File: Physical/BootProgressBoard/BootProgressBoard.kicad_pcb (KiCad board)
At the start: 2 copper layers, 49.5 x 28.6 mm, 12 parts, among them P1 CONN_01X09

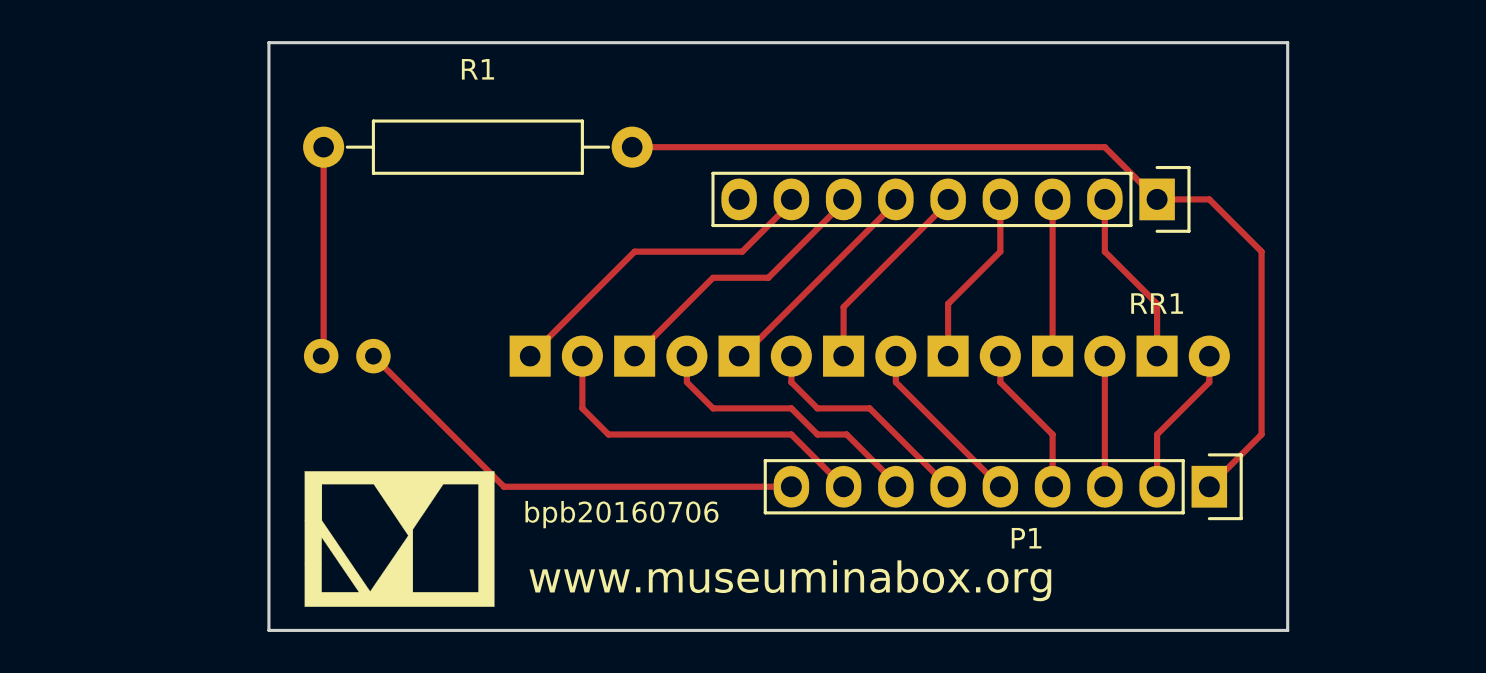
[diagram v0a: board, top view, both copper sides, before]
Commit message: Drop www. from URL, move logo & URL
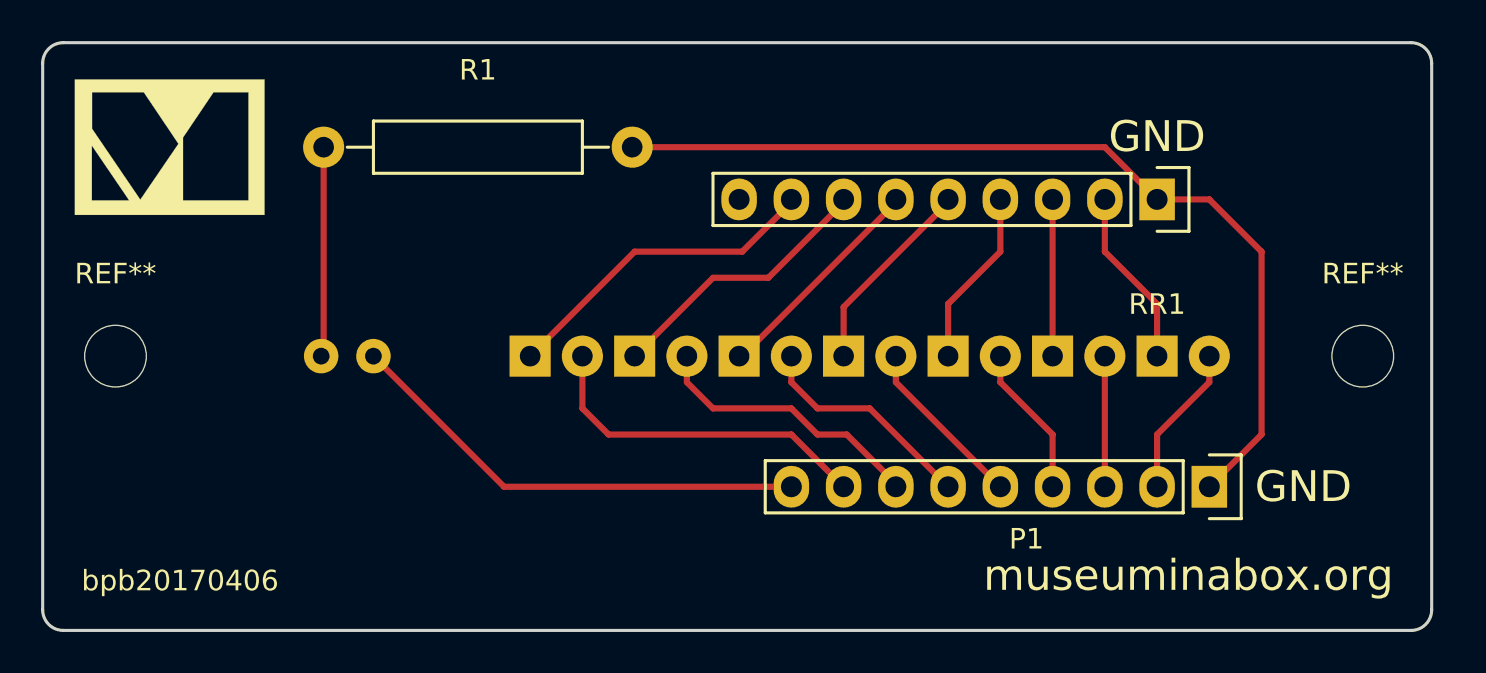
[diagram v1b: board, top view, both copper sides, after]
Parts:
- added G***: LOGO, MCQN Ltd:miab-logo-9x7mm, B.Cu at (154.4, 43.2)
- added REF**: MountingHole_3mm, Mounting_Holes:MountingHole_3mm, F.Cu at (96.7, 53.3)
- added REF**: MountingHole_3mm, Mounting_Holes:MountingHole_3mm, F.Cu at (157.3, 53.3)
- moved G*** 22.1 mm to (99.3, 43.2)
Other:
- board size 49.5 x 28.6 mm -> 67.5 x 28.6 mm
- board text added: "GND"
- board text added: "bpb20170406"
- board text added: "museuminabox.org"
- board text removed: "bpb20160706"
- board text removed: "www.museuminabox.org"
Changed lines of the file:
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@@
-(kicad_pcb (version 4) (host pcbnew 4.1.0-alpha+201607021448+6961~45~ubuntu15.04.1-product)
+(kicad_pcb (version 20170123) (host pcbnew no-vcs-found-1e25c47~58~ubuntu16.04.1)
   (general
-    (links 0)
+    (links 18)
     (no_connects 0)
-    (area 103.864999 38.024999 153.745001 66.750001)
+    (area 90.191475 38.024999 165.810046 66.750001)
     (thickness 1.6)
-    (drawings 6)
+    (drawings 13)
     (tracks 55)
     (zones 0)
-    (modules 12)
+    (modules 15)
     (nets 19)
   )
@@
     (trace_min 0.2)
     (segment_width 0.2)
-    (edge_width 0.15)
+    (edge_width 0.2)
     (via_size 0.8)
     (via_drill 0.4)
@@
     (add_net "Net-(RR1-Pad9)")
   )
+  (module Mounting_Holes:MountingHole_3mm (layer F.Cu)
+    (at 96.68 53.34)
+    (descr "Mounting hole, Befestigungsbohrung, 3mm, No Annular, Kein Restring,")
+    (tags "Mounting hole, Befestigungsbohrung, 3mm, No Annular, Kein Restring,")
+    (fp_text reference REF** (at 0 -4.0005) (layer F.SilkS)
+      (effects (font (size 1 1) (thickness 0.15)))
+    )
+    (fp_text value MountingHole_3mm (at 1.00076 5.00126) (layer F.Fab)
+      (effects (font (size 1 1) (thickness 0.15)))
+    )
+    (fp_circle (center 0 0) (end 3 0) (layer Cmts.User) (width 0.381))
+    (pad 1 thru_hole circle (at 0 0) (size 3 3) (drill 3) (layers))
+  )
+  (module Mounting_Holes:MountingHole_3mm (layer F.Cu)
+    (at 157.32 53.34)
+    (descr "Mounting hole, Befestigungsbohrung, 3mm, No Annular, Kein Restring,")
+    (tags "Mounting hole, Befestigungsbohrung, 3mm, No Annular, Kein Restring,")
+    (fp_text reference REF** (at 0 -4.0005) (layer F.SilkS)
+      (effects (font (size 1 1) (thickness 0.15)))
+    )
+    (fp_text value MountingHole_3mm (at 1.00076 5.00126) (layer F.Fab)
+      (effects (font (size 1 1) (thickness 0.15)))
+    )
+    (fp_circle (center 0 0) (end 3 0) (layer Cmts.User) (width 0.381))
+    (pad 1 thru_hole circle (at 0 0) (size 3 3) (drill 3) (layers))
+  )
+  (module "MCQN Ltd:miab-logo-9x7mm" (layer B.Cu)
+    (at 154.432 43.18 180)
+    (fp_text reference G*** (at 0 0 180) (layer B.SilkS) hide
+      (effects (font (thickness 0.3)) (justify mirror))
+    )
+    (fp_text value LOGO (at 0.75 0 180) (layer B.SilkS) hide
+      (effects (font (thickness 0.3)) (justify mirror))
+    )
+    (fp_poly (pts (xy 4.611512 -3.293533) (xy -4.608688 -3.293533) (xy -4.608688 -1.255324) (xy -3.7846 -1.255324)
+      (xy -3.7846 -2.587977) (xy -1.969262 -2.587977) (xy -1.973457 -2.581627) (xy -1.976057 -2.577762)
+      (xy -1.981691 -2.569442) (xy -1.990252 -2.556826) (xy -2.001629 -2.540074) (xy -2.015714 -2.519346)
+      (xy -2.032398 -2.494802) (xy -2.051573 -2.466603) (xy -2.073129 -2.434907) (xy -2.096958 -2.399875)
+      (xy -2.122951 -2.361666) (xy -2.150998 -2.32044) (xy -2.180992 -2.276358) (xy -2.212823 -2.229579)
+      (xy -2.246382 -2.180263) (xy -2.281561 -2.128569) (xy -2.318251 -2.074658) (xy -2.356342 -2.01869)
+      (xy -2.395727 -1.960824) (xy -2.436296 -1.901221) (xy -2.477941 -1.840039) (xy -2.520551 -1.777439)
+      (xy -2.56402 -1.713582) (xy -2.608238 -1.648626) (xy -2.653095 -1.582731) (xy -2.698484 -1.516058)
+      (xy -2.744295 -1.448767) (xy -2.790419 -1.381016) (xy -2.836749 -1.312966) (xy -2.883174 -1.244778)
+      (xy -2.929586 -1.17661) (xy -2.975876 -1.108622) (xy -3.021935 -1.040975) (xy -3.067655 -0.973829)
+      (xy -3.112927 -0.907342) (xy -3.157641 -0.841676) (xy -3.201689 -0.77699) (xy -3.244963 -0.713443)
+      (xy -3.287353 -0.651196) (xy -3.32875 -0.590408) (xy -3.369045 -0.53124) (xy -3.408131 -0.473851)
+      (xy -3.445897 -0.418401) (xy -3.482235 -0.36505) (xy -3.517037 -0.313958) (xy -3.550193 -0.265285)
+      (xy -3.581594 -0.21919) (xy -3.611132 -0.175833) (xy -3.638698 -0.135375) (xy -3.664183 -0.097975)
+      (xy -3.687478 -0.063793) (xy -3.708475 -0.032988) (xy -3.727064 -0.005722) (xy -3.743137 0.017847)
+      (xy -3.756584 0.037559) (xy -3.767297 0.053253) (xy -3.775168 0.06477) (xy -3.780087 0.07195)
+      (xy -3.781945 0.074634) (xy -3.781957 0.074648) (xy -3.782166 0.072056) (xy -3.782367 0.063907)
+      (xy -3.782562 0.050287) (xy -3.782748 0.031283) (xy -3.782927 0.006984) (xy -3.783097 -0.022526)
+      (xy -3.78326 -0.057158) (xy -3.783414 -0.096825) (xy -3.783559 -0.141441) (xy -3.783696 -0.190918)
+      (xy -3.783823 -0.24517) (xy -3.783942 -0.304109) (xy -3.784052 -0.367649) (xy -3.784152 -0.435702)
+      (xy -3.784242 -0.508182) (xy -3.784323 -0.585002) (xy -3.784393 -0.666074) (xy -3.784454 -0.751312)
+      (xy -3.784504 -0.840628) (xy -3.784544 -0.933936) (xy -3.784574 -1.031148) (xy -3.784592 -1.132178)
+      (xy -3.784599 -1.236939) (xy -3.7846 -1.255324) (xy -4.608688 -1.255324) (xy -4.608688 0.897932)
+      (xy -3.773311 0.897932) (xy -2.629958 -0.783639) (xy -2.569622 -0.872377) (xy -2.509994 -0.960073)
+      (xy -2.451157 -1.046605) (xy -2.393193 -1.131853) (xy -2.336183 -1.215697) (xy -2.280209 -1.298017)
+      (xy -2.225353 -1.378691) (xy -2.171698 -1.457601) (xy -2.119324 -1.534624) (xy -2.068314 -1.609641)
+      (xy -2.01875 -1.682532) (xy -1.970713 -1.753175) (xy -1.924286 -1.82145) (xy -1.87955 -1.887238)
+      (xy -1.836588 -1.950417) (xy -1.79548 -2.010867) (xy -1.75631 -2.068468) (xy -1.719159 -2.123099)
+      (xy -1.684109 -2.17464) (xy -1.651241 -2.222971) (xy -1.620639 -2.26797) (xy -1.592382 -2.309518)
+      (xy -1.566555 -2.347493) (xy -1.543238 -2.381777) (xy -1.522512 -2.412247) (xy -1.504462 -2.438785)
+      (xy -1.489167 -2.461268) (xy -1.47671 -2.479578) (xy -1.467173 -2.493593) (xy -1.460638 -2.503193)
+      (xy -1.457187 -2.508257) (xy -1.457017 -2.508506) (xy -1.447611 -2.52199) (xy -1.43921 -2.533505)
+      (xy -1.43234 -2.542373) (xy -1.427529 -2.547912) (xy -1.425306 -2.549441) (xy -1.425294 -2.549429)
+      (xy -1.423592 -2.546979) (xy -1.418799 -2.539996) (xy -1.411003 -2.528609) (xy -1.400291 -2.512949)
+      (xy -1.386754 -2.493144) (xy -1.370479 -2.469326) (xy -1.351554 -2.441622) (xy -1.33007 -2.410164)
+      (xy -1.306113 -2.375081) (xy -1.279772 -2.336503) (xy -1.251137 -2.294559) (xy -1.220296 -2.249379)
+      (xy -1.187337 -2.201094) (xy -1.152348 -2.149832) (xy -1.115419 -2.095723) (xy -1.076638 -2.038898)
+      (xy -1.036094 -1.979486) (xy -0.993874 -1.917617) (xy -0.950068 -1.85342) (xy -0.904765 -1.787026)
+      (xy -0.858052 -1.718563) (xy -0.810018 -1.648163) (xy -0.760753 -1.575954) (xy -0.710343 -1.502066)
+      (xy -0.658879 -1.42663) (xy -0.606449 -1.349774) (xy -0.55314 -1.271629) (xy -0.499042 -1.192324)
+      (xy -0.49845 -1.191456) (xy 0.426258 0.164143) (xy 0.377524 0.23677) (xy 0.37286 0.243715)
+      (xy 0.365146 0.255192) (xy 0.354486 0.271049) (xy 0.340981 0.291135) (xy 0.324732 0.315298)
+      (xy 0.305842 0.343388) (xy 0.284412 0.375252) (xy 0.260544 0.410739) (xy 0.234341 0.449698)
+      (xy 0.223481 0.465845) (xy 0.649112 0.465845) (xy 0.649112 -2.587977) (xy 3.832578 -2.587977)
+      (xy 3.832578 2.667) (xy 2.131737 2.667) (xy 1.390424 1.566423) (xy 0.649112 0.465845)
+      (xy 0.223481 0.465845) (xy 0.205903 0.491978) (xy 0.175333 0.537426) (xy 0.142733 0.585892)
+      (xy 0.108205 0.637223) (xy 0.07185 0.69127) (xy 0.03377 0.747879) (xy -0.005932 0.8069)
+      (xy -0.047156 0.868182) (xy -0.089799 0.931572) (xy -0.133759 0.99692) (xy -0.178934 1.064074)
+      (xy -0.225223 1.132882) (xy -0.272524 1.203194) (xy -0.320734 1.274857) (xy -0.369753 1.347721)
+      (xy -0.419477 1.421633) (xy -0.464255 1.488192) (xy -1.2573 2.666986) (xy -2.515305 2.666993)
+      (xy -3.773311 2.667) (xy -3.773311 0.897932) (xy -4.608688 0.897932) (xy -4.608688 3.290711)
+      (xy 4.611512 3.290711) (xy 4.611512 -3.293533)) (layer B.SilkS) (width 0.01))
+  )
   (module LEDs:LED-8MM (layer B.Cu)
     (at 106.68 53.34)
@@
   )
   (module "MCQN Ltd:miab-logo-9x7mm" (layer F.Cu)
-    (at 110.49 62.23)
+    (at 99.314 43.18)
     (fp_text reference G*** (at 0 0) (layer F.SilkS) hide
       (effects (font (thickness 0.3)))
@@
       (xy 4.611512 -3.290711) (xy 4.611512 3.293533)) (layer F.SilkS) (width 0.01))
   )
-  (gr_text www.museuminabox.org (at 129.54 64.135) (layer F.SilkS)
+  (gr_text GND (at 147.32 42.672) (layer F.SilkS)
     (effects (font (size 1.5 1.5) (thickness 0.3)))
   )
-  (gr_text bpb20160706 (at 121.285 60.96) (layer F.SilkS)
+  (gr_text GND (at 154.432 59.69) (layer F.SilkS)
+    (effects (font (size 1.5 1.5) (thickness 0.3)))
+  )
+  (gr_text museuminabox.org (at 104.902 64.008) (layer B.SilkS)
+    (effects (font (size 1.5 1.5) (thickness 0.3)) (justify mirror))
+  )
+  (gr_arc (start 159.67 39.1) (end 159.67 38.1) (angle 90) (layer Edge.Cuts) (width 0.15))
+  (gr_arc (start 159.67 65.675) (end 159.67 66.675) (angle -90) (layer Edge.Cuts) (width 0.15))
+  (gr_arc (start 94.14 65.675) (end 93.14 65.675) (angle -90) (layer Edge.Cuts) (width 0.15))
+  (gr_arc (start 94.14 39.1) (end 93.14 39.1) (angle 90) (layer Edge.Cuts) (width 0.15))
+  (gr_text museuminabox.org (at 148.844 64.008) (layer F.SilkS)
+    (effects (font (size 1.5 1.5) (thickness 0.3)))
+  )
+  (gr_text bpb20170406 (at 99.822 64.262) (layer F.SilkS)
     (effects (font (size 1 1) (thickness 0.25)))
   )
-  (gr_line (start 104.14 66.675) (end 104.14 38.1) (layer Edge.Cuts) (width 0.15))
-  (gr_line (start 153.67 66.675) (end 104.14 66.675) (layer Edge.Cuts) (width 0.15))
-  (gr_line (start 153.67 38.1) (end 153.67 66.675) (layer Edge.Cuts) (width 0.15))
-  (gr_line (start 104.14 38.1) (end 153.67 38.1) (layer Edge.Cuts) (width 0.15))
+  (gr_line (start 93.14 65.675) (end 93.14 39.1) (layer Edge.Cuts) (width 0.15))
+  (gr_line (start 159.67 66.675) (end 94.14 66.675) (layer Edge.Cuts) (width 0.15))
+  (gr_line (start 160.67 39.1) (end 160.67 65.675) (layer Edge.Cuts) (width 0.15))
+  (gr_line (start 94.14 38.1) (end 159.67 38.1) (layer Edge.Cuts) (width 0.15))
   (segment (start 129.54 59.69) (end 115.57 59.69) (width 0.3) (layer F.Cu) (net 1))
   (segment (start 115.57 59.69) (end 109.22 53.34) (width 0.3) (layer F.Cu) (net 1))
